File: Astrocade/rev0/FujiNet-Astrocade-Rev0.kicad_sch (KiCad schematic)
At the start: 0 parts

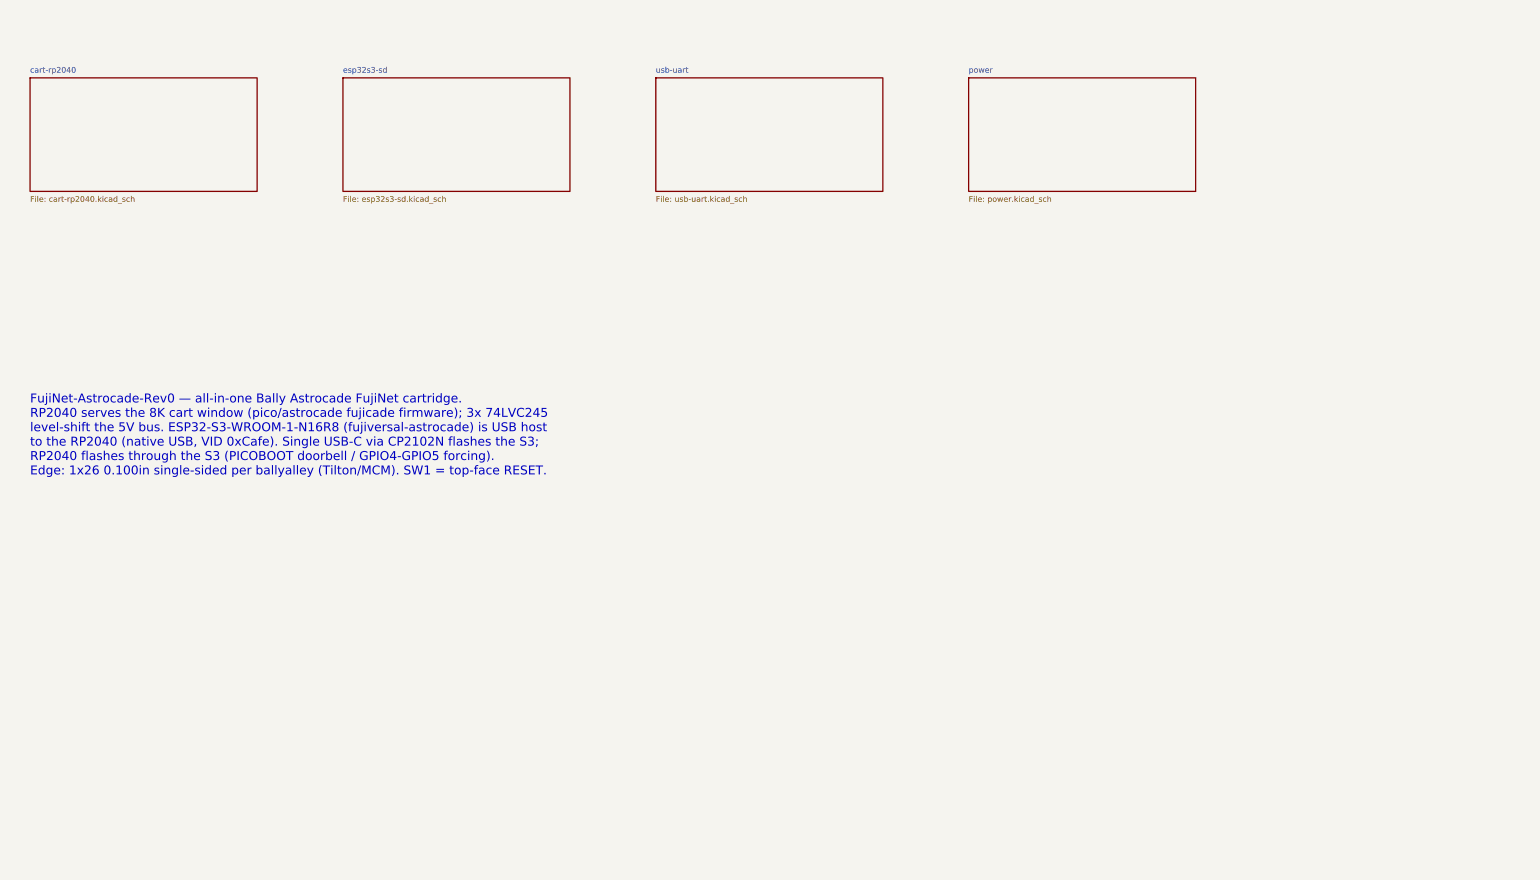
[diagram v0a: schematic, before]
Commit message: Astrocade Rev0: redo on RP2354A + ESP32-S3, 6-layer, fully autorouted
Replaces the unrouted RP2040 + 3x LVC245 draft with an INTV-style board:
RP2354A straight on the 5V bus, ESP32-S3-WROOM-1-N16R8 as its USB host
(PICOBOOT reflash), USB-C/CP2102N, push-push microSD, WS2812B-2020-V6,
RESET/BOOTSEL/EN/BOOT buttons. Same cassette outline, lands and holes.

Everything is generated by tools/ (build_all.sh): design.py -> schematic,
placement + plane fan-out, Raspberry Pi's MIT regulator-corner graft,
Freerouting + A* finisher, netlist-vs-firmware check, JLCPCB BOM/CPL/gerbers.
ERC 0, DRC 0 errors / 0 unconnected / 0 parity, check_nets 174/174.

RUN/BOOTSEL from the S3 are direct 1k links (fnPicoUpdater drives them low;
an NPN driver would invert it). Shell openings come from the placement.

Co-Authored-By: Claude Opus 5.5 (1M context) <noreply@anthropic.com>
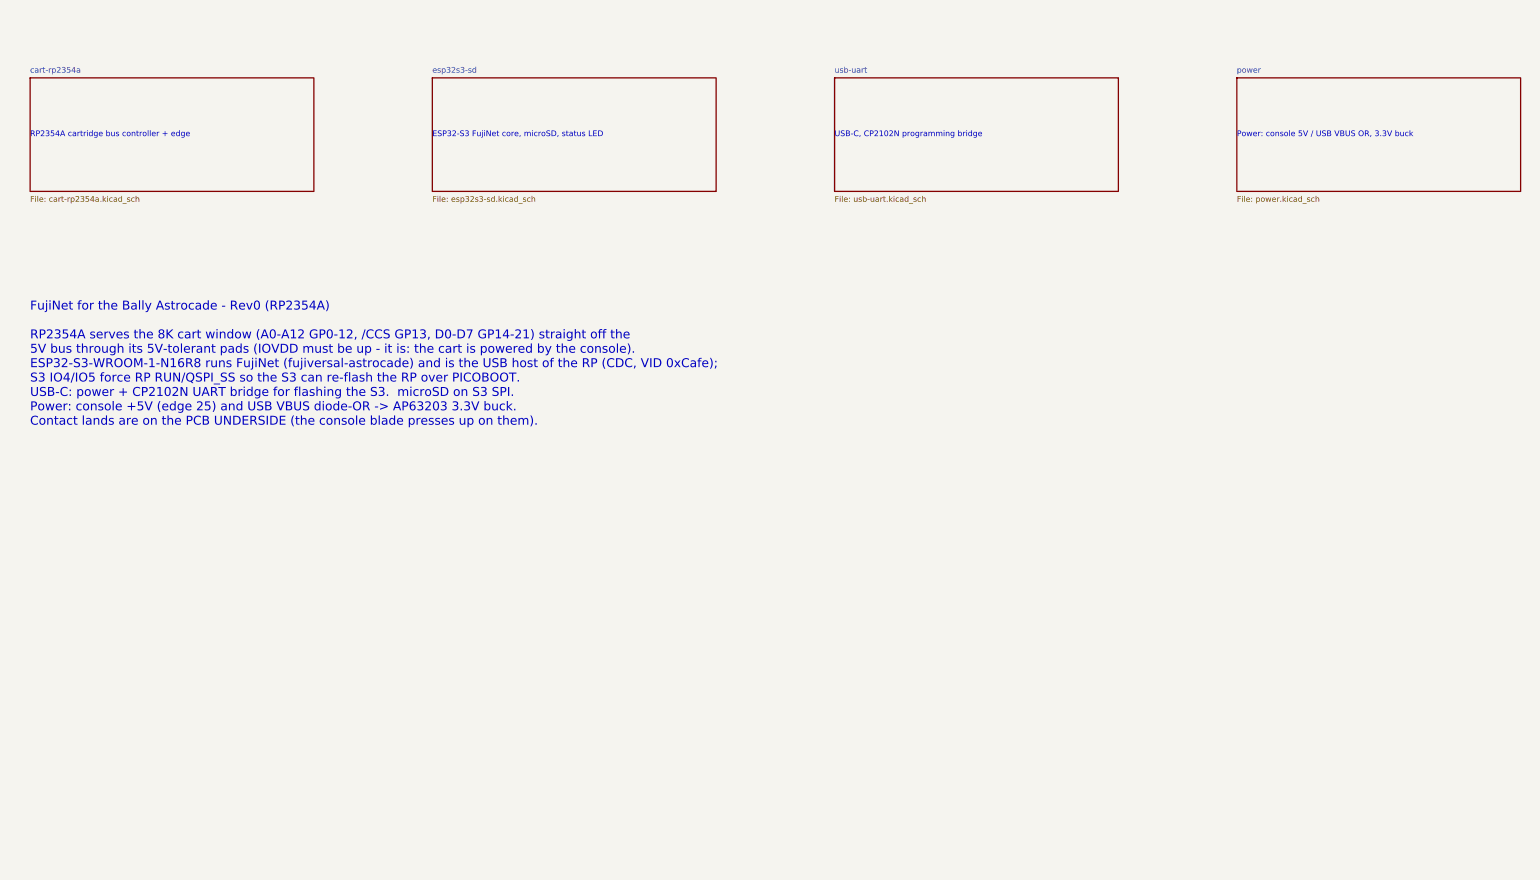
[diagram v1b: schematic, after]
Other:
- removed sheet cart-rp2040
- added sheet cart-rp2354a (cart-rp2354a.kicad_sch)
- note added: "ESP32-S3 FujiNet core, microSD, status LED"
- note added: "FujiNet for the Bally Astrocade - Rev0 (RP2354A) RP2354A serves the 8K cart window (A0-A12 GP0-12, /CCS GP13, D0-D7 GP14-21) straight off the 5V bus through its 5V-tolerant pads (IOVDD must be up - it is: the cart is powered by the console). ESP32-S3-WROOM-1-N16R8 runs FujiNet (fujiversal-astrocade) and is the USB host of the RP (CDC, VID 0xCafe); S3 IO4/IO5 force RP RUN/QSPI_SS so the S3 can re-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"
- note added: "Power: console 5V / USB VBUS OR, 3.3V buck"
- note added: "RP2354A cartridge bus controller + edge"
- note added: "USB-C, CP2102N programming bridge"
- note removed: "FujiNet-Astrocade-Rev0 — all-in-one Bally Astrocade FujiNet cartridge. RP2040 serves the 8K cart window (pico/astrocade fujicade firmware); 3x 74LVC245 level-shift the 5V bus. ESP32-S3-WROOM-1-N16R8 (fujiversal-astrocade) is USB host to the RP2040 (native USB, VID 0xCafe). Single USB-C via CP2102N flashes the S3; RP2040 flashes through the S3 (PICOBOOT doorbell / GPIO4-GPIO5 forcing). Edge: 1x26 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"
- company: (none) -> FujiNet
- title: (none) -> FujiNet Astrocade Rev0
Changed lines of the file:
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@@
 	(generator_version "9.0")
 	(paper "A3")
+	(title_block
+		(title "FujiNet Astrocade Rev0")
+		(date "2026-09-26")
+		(rev "0")
+		(company "FujiNet")
+		(comment 1 "Generated by tools/gen_sch.py")
+	)
 	(sheet
 		(at 30 40)
-		(size 50.8 25.4)
-		(fields_autoplaced yes)
-		(stroke
-			(width 0.12)
-			(type solid)
-		)
-		(fill
-			(color 0 0 0 0.0000)
-		)
-		(property "Sheetname" "cart-rp2040"
+		(size 63.5 25.4)
+		(fields_autoplaced yes)
+		(stroke
+			(width 0.12)
+			(type solid)
+		)
+		(fill
+			(color 0 0 0 0)
+		)
+		(property "Sheetname" "cart-rp2354a"
 			(at 30 39 0)
 			(effects
@@
 			)
 		)
-		(property "Sheetfile" "cart-rp2040.kicad_sch"
+		(property "Sheetfile" "cart-rp2354a.kicad_sch"
 			(at 30 66.4 0)
 			(effects
@@
 		(instances
 			(project "FujiNet-Astrocade-Rev0"
-				(path "/892e4e06-ac77-5e44-a273-1b91db5e02f7"
+				(path "/16a46450-576a-5590-8e32-77c1aaabfa76"
 					(page "2")
 				)
@@
 		)
 	)
-	(sheet
-		(at 100 40)
-		(size 50.8 25.4)
-		(fields_autoplaced yes)
-		(stroke
-			(width 0.12)
-			(type solid)
-		)
-		(fill
-			(color 0 0 0 0.0000)
+	(text "RP2354A cartridge bus controller + edge"
+		(exclude_from_sim no)
+		(at 30 52.7 0)
+		(effects
+			(font
+				(size 1.27 1.27)
+			)
+			(justify left)
+		)
+	)
+	(sheet
+		(at 120 40)
+		(size 63.5 25.4)
+		(fields_autoplaced yes)
+		(stroke
+			(width 0.12)
+			(type solid)
+		)
+		(fill
+			(color 0 0 0 0)
 		)
 		(property "Sheetname" "esp32s3-sd"
-			(at 100 39 0)
+			(at 120 39 0)
 			(effects
 				(font
@@
 		)
 		(property "Sheetfile" "esp32s3-sd.kicad_sch"
-			(at 100 66.4 0)
-			(effects
-				(font
-					(size 1.27 1.27)
-				)
-				(justify left top)
-			)
-		)
-		(instances
-			(project "FujiNet-Astrocade-Rev0"
-				(path "/892e4e06-ac77-5e44-a273-1b91db5e02f7"
+			(at 120 66.4 0)
+			(effects
+				(font
+					(size 1.27 1.27)
+				)
+				(justify left top)
+			)
+		)
+		(instances
+			(project "FujiNet-Astrocade-Rev0"
+				(path "/16a46450-576a-5590-8e32-77c1aaabfa76"
 					(page "3")
 				)
@@
 		)
 	)
-	(sheet
-		(at 170 40)
-		(size 50.8 25.4)
-		(fields_autoplaced yes)
-		(stroke
-			(width 0.12)
-			(type solid)
-		)
-		(fill
-			(color 0 0 0 0.0000)
+	(text "ESP32-S3 FujiNet core, microSD, status LED"
+		(exclude_from_sim no)
+		(at 120 52.7 0)
+		(effects
+			(font
+				(size 1.27 1.27)
+			)
+			(justify left)
+		)
+	)
+	(sheet
+		(at 210 40)
+		(size 63.5 25.4)
+		(fields_autoplaced yes)
+		(stroke
+			(width 0.12)
+			(type solid)
+		)
+		(fill
+			(color 0 0 0 0)
 		)
 		(property "Sheetname" "usb-uart"
-			(at 170 39 0)
+			(at 210 39 0)
 			(effects
 				(font
@@
 		)
 		(property "Sheetfile" "usb-uart.kicad_sch"
-			(at 170 66.4 0)
-			(effects
-				(font
-					(size 1.27 1.27)
-				)
-				(justify left top)
-			)
-		)
-		(instances
-			(project "FujiNet-Astrocade-Rev0"
-				(path "/892e4e06-ac77-5e44-a273-1b91db5e02f7"
+			(at 210 66.4 0)
+			(effects
+				(font
+					(size 1.27 1.27)
+				)
+				(justify left top)
+			)
+		)
+		(instances
+			(project "FujiNet-Astrocade-Rev0"
+				(path "/16a46450-576a-5590-8e32-77c1aaabfa76"
 					(page "4")
 				)
@@
 		)
 	)
-	(sheet
-		(at 240 40)
-		(size 50.8 25.4)
-		(fields_autoplaced yes)
-		(stroke
-			(width 0.12)
-			(type solid)
-		)
-		(fill
-			(color 0 0 0 0.0000)
+	(text "USB-C, CP2102N programming bridge"
+		(exclude_from_sim no)
+		(at 210 52.7 0)
+		(effects
+			(font
+				(size 1.27 1.27)
+			)
+			(justify left)
+		)
+	)
+	(sheet
+		(at 300 40)
+		(size 63.5 25.4)
+		(fields_autoplaced yes)
+		(stroke
+			(width 0.12)
+			(type solid)
+		)
+		(fill
+			(color 0 0 0 0)
 		)
 		(property "Sheetname" "power"
-			(at 240 39 0)
+			(at 300 39 0)
 			(effects
 				(font
@@
 		)
 		(property "Sheetfile" "power.kicad_sch"
-			(at 240 66.4 0)
-			(effects
-				(font
-					(size 1.27 1.27)
-				)
-				(justify left top)
-			)
-		)
-		(instances
-			(project "FujiNet-Astrocade-Rev0"
-				(path "/892e4e06-ac77-5e44-a273-1b91db5e02f7"
+			(at 300 66.4 0)
+			(effects
+				(font
+					(size 1.27 1.27)
+				)
+				(justify left top)
+			)
+		)
+		(instances
+			(project "FujiNet-Astrocade-Rev0"
+				(path "/16a46450-576a-5590-8e32-77c1aaabfa76"
 					(page "5")
 				)
@@
 		)
 	)
-	(text "FujiNet-Astrocade-Rev0 — all-in-one Bally Astrocade FujiNet cartridge.\nRP2040 serves the 8K cart window (pico/astrocade fujicade firmware); 3x 74LVC245\nlevel-shift the 5V bus. ESP32-S3-WROOM-1-N16R8 (fujiversal-astrocade) is USB host\nto the RP2040 (native USB, VID 0xCafe). Single USB-C via CP2102N flashes the S3;\nRP2040 flashes through the S3 (PICOBOOT doorbell / GPIO4-GPIO5 forcing).\nEdge: 1x26 0.100in single-sided per ballyalley (Tilton/MCM). SW1 = top-face RESET."
-		(exclude_from_sim no)
-		(at 30 120 0)
+	(text "Power: console 5V / USB VBUS OR, 3.3V buck"
+		(exclude_from_sim no)
+		(at 300 52.7 0)
+		(effects
+			(font
+				(size 1.27 1.27)
+			)
+			(justify left)
+		)
+	)
+	(text "FujiNet for the Bally Astrocade - Rev0 (RP2354A)\n\nRP2354A serves the 8K cart window (A0-A12 GP0-12, /CCS GP13, D0-D7 GP14-21) straight off the\n5V bus through its 5V-tolerant pads (IOVDD must be up - it is: the cart is powered by the console).\nESP32-S3-WROOM-1-N16R8 runs FujiNet (fujiversal-astrocade) and is the USB host of the RP (CDC, VID 0xCafe);\nS3 IO4/IO5 force RP RUN/QSPI_SS so the S3 can re-flash the RP over PICOBOOT.\nUSB-C: power + CP2102N UART bridge for flashing the S3.  microSD on S3 SPI.\nPower: console +5V (edge 25) and USB VBUS diode-OR -> AP63203 3.3V buck.\nContact lands are on the PCB UNDERSIDE (the console blade presses up on them)."
+		(exclude_from_sim no)
+		(at 30 90 0)
 		(effects
 			(font
 				(size 2 2)
 			)
-			(justify left)
+			(justify left top)
 		)
 	)
@@
 		)
 	)
+	(embedded_fonts no)
 )

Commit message: Astrocade Rev0: audit with kicad-happy + datasheets and redo
Schematic, board and fab outputs regenerated from tools/ after a
datasheet-level audit (docs/design-review-rev0.md).

Design fixes:
- RP2354A on its own AP2112K rail (+3V3_RP): its FT pads take 5.5 V only
  with IOVDD powered (RP2350 DS p.1332); the buck's UVLO + 4 ms soft-start
  left them unpowered while the console drove the bus
- WS2812B-2020-V6 on +5V (datasheet VDD 3.7-5.3 V, not a 3.3 V part)
- VBUS decoupling at the USB-C, activity LED 330R, card-detect polarity
  settled (low = card present), fiducials, RUN/BOOTSEL/rail test pads

Schematic redrawn readably: root block diagram with hierarchical pins,
power symbols, wired clusters and design notes (tools/sch_layout.py);
check_sch_layout.py proves the drawn netlist equals design.py.

Board: 4 layers tried first and did not close; 6 layers, 100% routed,
DRC 0 errors / 0 unconnected / 0 parity. Locked USB-C D+/D- pad ties,
GND stitching kept out of pads, return vias at USB/crystal layer
changes, check_vias.py gate (KiCad re-nets a via inside another net's
pad, so its DRC cannot see it).

Co-Authored-By: Claude Opus 5.5 <noreply@anthropic.com>
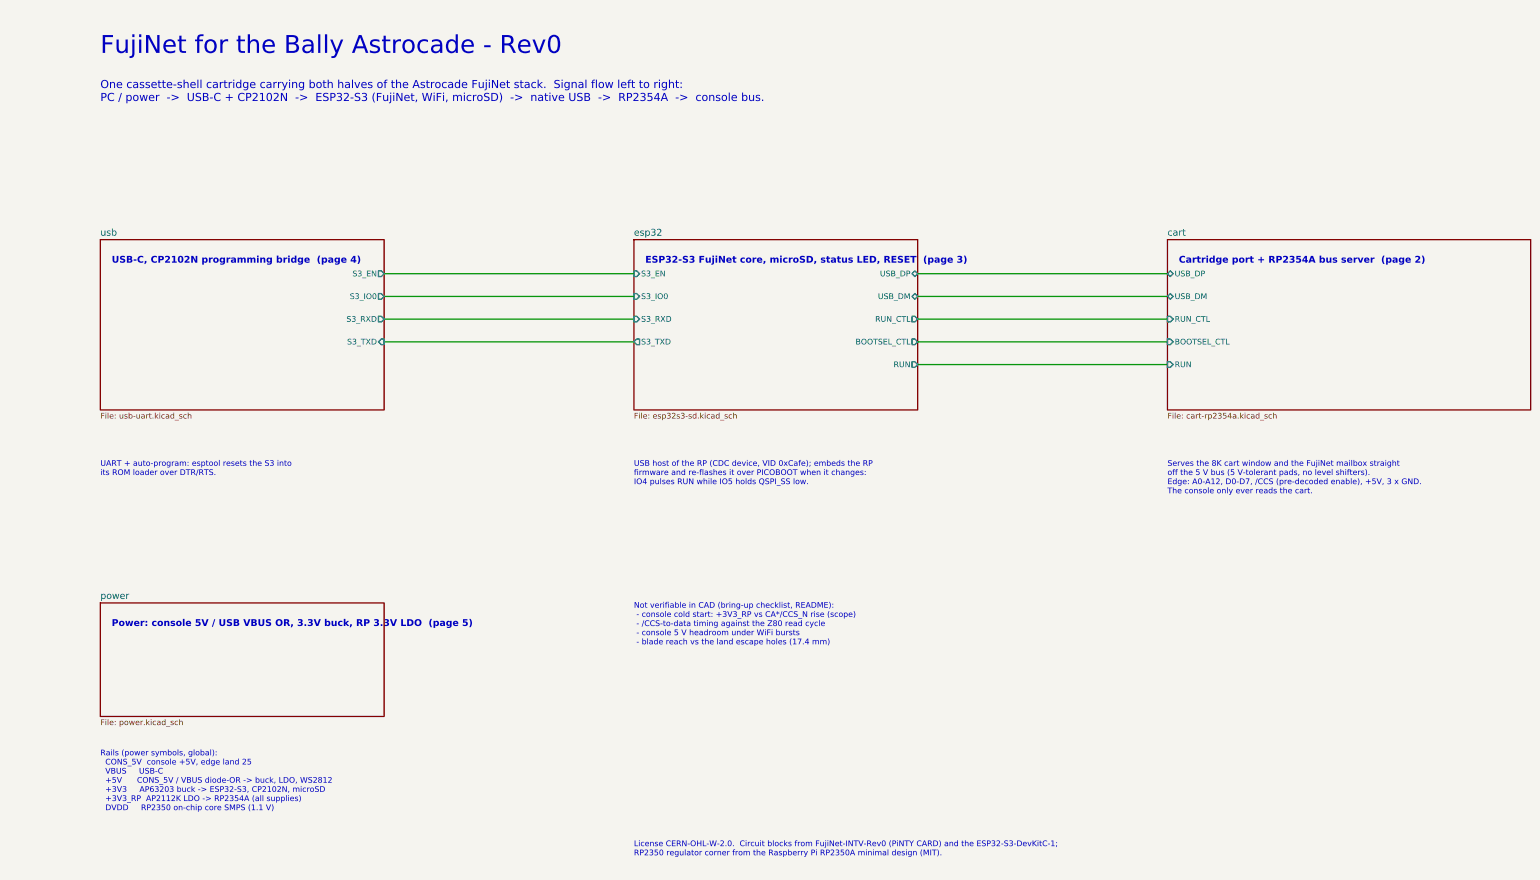
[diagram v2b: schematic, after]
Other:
- sheet cart-rp2354a renamed cart
- sheet esp32s3-sd renamed esp32
- sheet usb-uart renamed usb
- sheet cart ports: added BOOTSEL_CTL, RUN, RUN_CTL, USB_DM, USB_DP; removed none
- sheet esp32 ports: added BOOTSEL_CTL, RUN, RUN_CTL, S3_EN, S3_IO0, S3_RXD, S3_TXD, USB_DM, USB_DP; removed none
- sheet usb ports: added S3_EN, S3_IO0, S3_RXD, S3_TXD; removed none
- note added: "Cartridge port + RP2354A bus server (page 2)"
- note added: "ESP32-S3 FujiNet core, microSD, status LED, RESET (page 3)"
- note added: "FujiNet for the Bally Astrocade - Rev0"
- note added: "License CERN-OHL-W-2.0. Circuit blocks from FujiNet-INTV-Rev0 (PiNTY CARD) and the ESP32-S3-DevKitC-1; RP2350 regulator corner from the Raspberry Pi RP2350A minimal design (MIT)."
- note added: "Not verifiable in CAD (bring-up checklist, README): - console cold start: +3V3_RP vs CA*/CCS_N rise (scope) - /CCS-to-data timing against the Z80 read cycle - console 5 V headroom under WiFi bursts - blade reach vs the land escape holes (17.4 mm)"
- note added: "One cassette-shell cartridge carrying both halves of the Astrocade FujiNet stack. Signal flow left to right: PC / power -> USB-C + CP2102N -> ESP32-S3 (FujiNet, WiFi, microSD) -> native USB -> RP2354A -> console bus."
- note added: "Power: console 5V / USB VBUS OR, 3.3V buck, RP 3.3V LDO (page 5)"
- note added: "Rails (power symbols, global): CONS_5V console +5V, edge land 25 VBUS USB-C +5V CONS_5V / VBUS diode-OR -> buck, LDO, WS2812 +3V3 AP63203 buck -> ESP32-S3, CP2102N, microSD +3V3_RP AP2112K LDO -> RP2354A (all supplies) DVDD RP2350 on-chip core SMPS (1.1 V)"
- note added: "Serves the 8K cart window and the FujiNet mailbox straight off the 5 V bus (5 V-tolerant pads, no level shifters). Edge: A0-A12, D0-D7, /CCS (pre-decoded enable), +5V, 3 x GND. The console only ever reads the cart."
- note added: "UART + auto-program: esptool resets the S3 into its ROM loader over DTR/RTS."
- note added: "USB host of the RP (CDC device, VID 0xCafe); embeds the RP firmware and re-flashes it over PICOBOOT when it changes: IO4 pulses RUN while IO5 holds QSPI_SS low."
- note added: "USB-C, CP2102N programming bridge (page 4)"
- note removed: "ESP32-S3 FujiNet core, microSD, status LED"
- note removed: "FujiNet for the Bally Astrocade - Rev0 (RP2354A) RP2354A serves the 8K cart window (A0-A12 GP0-12, /CCS GP13, D0-D7 GP14-21) straight off the 5V bus through its 5V-tolerant pads (IOVDD must be up - it is: the cart is powered by the console). ESP32-S3-WROOM-1-N16R8 runs FujiNet (fujiversal-astrocade) and is the USB host of the RP (CDC, VID 0xCafe); S3 IO4/IO5 force RP RUN/QSPI_SS so the S3 can re-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"
- note removed: "Power: console 5V / USB VBUS OR, 3.3V buck"
- note removed: "RP2354A cartridge bus controller + edge"
- note removed: "USB-C, CP2102N programming bridge"
